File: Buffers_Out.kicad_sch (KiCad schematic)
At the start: 37 parts, among them U6 NE5532, U7 NE5532, X1 PEDAL_COMBO_TOP

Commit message: Bias voltage fix
Fixed the label for the output bias voltage.
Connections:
- net VBIAS_OUT is gone; now on net +VBIAS_OUT: C34.2, C35.2, R21.2, R23.2, R28.2, R29.2
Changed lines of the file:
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@@
 		)
 	)
-	(global_label "VBIAS_OUT"
+	(global_label "+VBIAS_OUT"
 		(shape input)
 		(at 90.17 151.13 0)
@@
 		)
 		(property "Intersheetrefs" "${INTERSHEET_REFS}"
-			(at 103.0129 151.13 0)
+			(at 104.5853 151.13 0)
 			(effects
 				(font
@@
 		)
 	)
-	(global_label "VBIAS_OUT"
+	(global_label "+VBIAS_OUT"
 		(shape input)
 		(at 90.17 81.28 0)
@@
 		)
 		(property "Intersheetrefs" "${INTERSHEET_REFS}"
-			(at 103.0129 81.28 0)
+			(at 104.5853 81.28 0)
 			(effects
 				(font

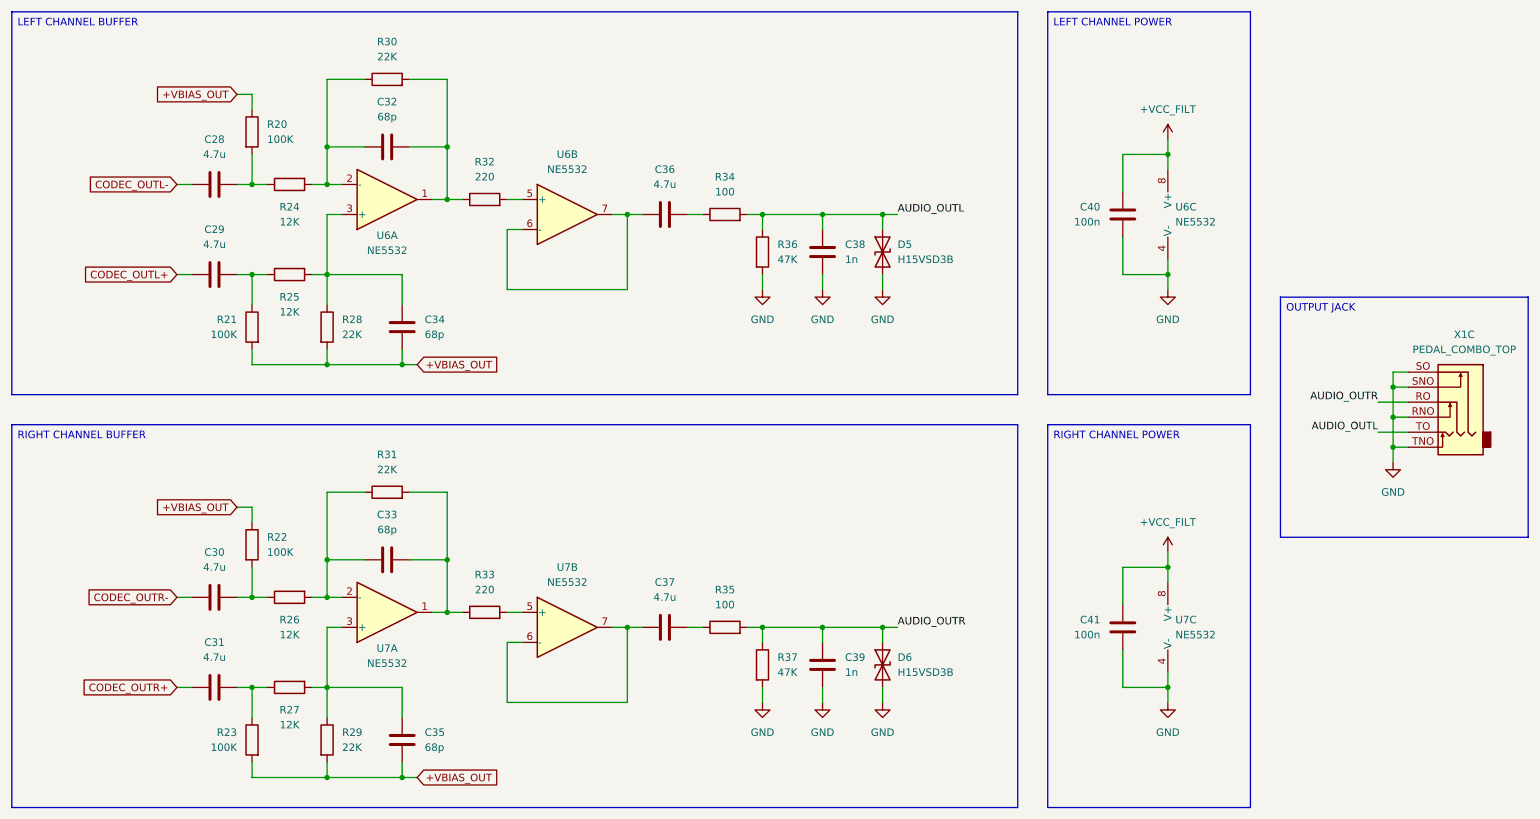
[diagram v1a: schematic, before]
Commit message: Buffer and layout
Updated the input and output buffers.
Updated the board layout.
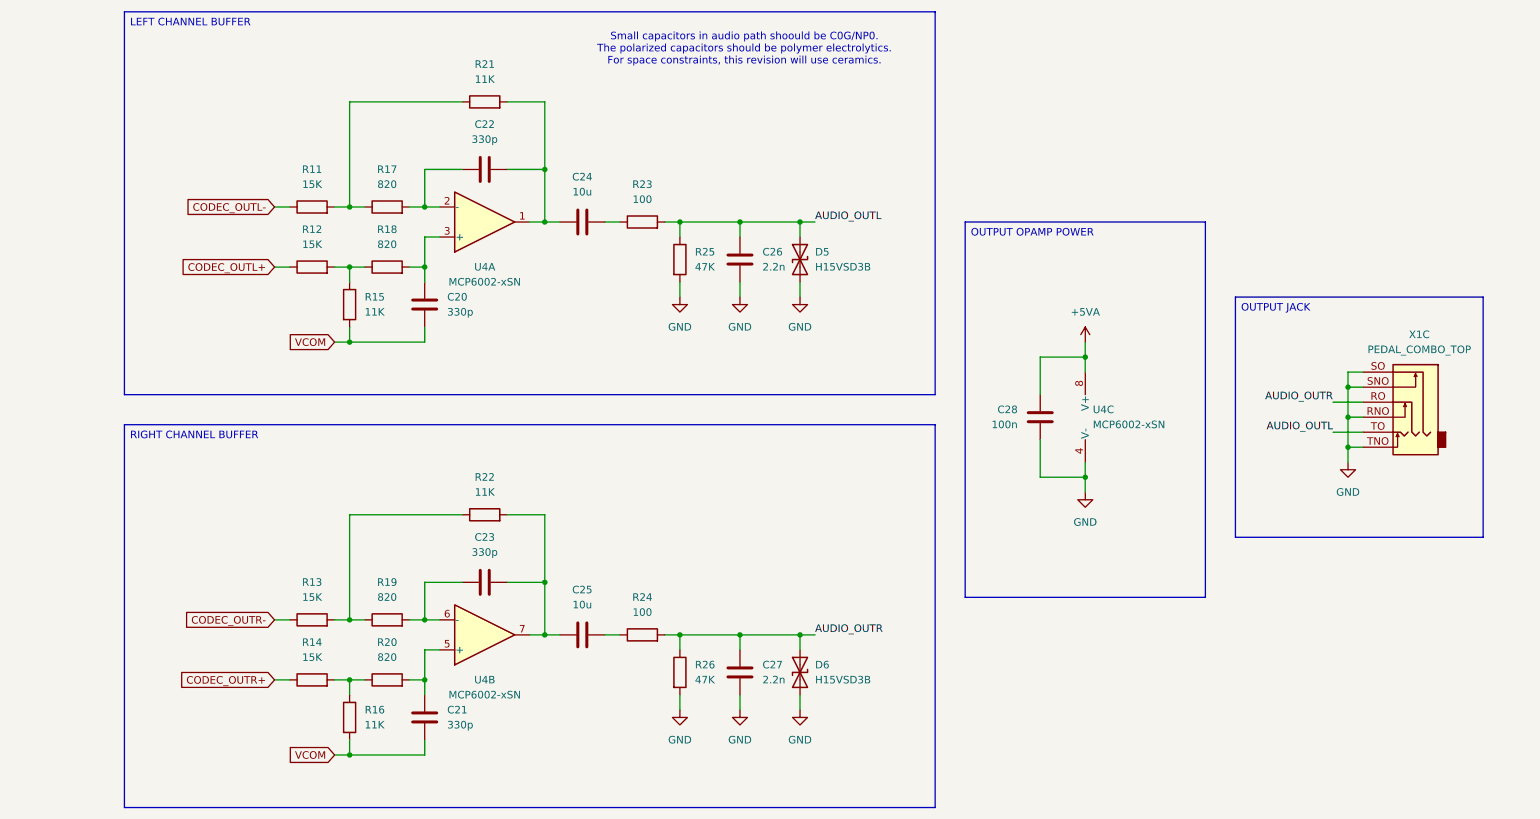
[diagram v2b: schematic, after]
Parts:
- removed C29, C30, C31, C36, C37: 4.7u, Capacitor_SMD:C_1206_3216Metric, symbol Device:C
- removed C32, C33, C34, C35: 68p, Capacitor_SMD:C_0603_1608Metric, symbol Device:C
- removed C38, C39: 1n, Capacitor_SMD:C_0603_1608Metric, symbol Device:C
- removed C40, C41: 100n, Capacitor_SMD:C_0603_1608Metric, symbol Device:C
- removed R27: 12K, Resistor_SMD:R_0603_1608Metric, symbol Device:R
- removed R28, R29, R30, R31: 22K, Resistor_SMD:R_0603_1608Metric, symbol Device:R
- removed R32, R33: 220, Resistor_SMD:R_0603_1608Metric, symbol Device:R
- removed R34, R35: 100, Resistor_SMD:R_0603_1608Metric, symbol Device:R
- removed R36, R37: 47K, Resistor_SMD:R_0603_1608Metric, symbol Device:R
- removed U6, U7: NE5532, Package_SO:SOIC-8_3.9x4.9mm_P1.27mm, symbol Amplifier_Operational:NE5532
- added C20, C21, C22, C23: 330p, Capacitor_SMD:C_0603_1608Metric, symbol Device:C
- added C24, C25: 10u, Capacitor_SMD:C_1206_3216Metric, symbol Device:C
- added C26, C27: 2.2n, Capacitor_SMD:C_0805_2012Metric, symbol Device:C
- added R11, R12, R13, R14: 15K, Resistor_SMD:R_0603_1608Metric, symbol Device:R
- added R15, R16: 11K, Resistor_SMD:R_0603_1608Metric, symbol Device:R
- added R17, R18, R19: 820, Resistor_SMD:R_0603_1608Metric, symbol Device:R
- added U4: MCP6002-xSN, Package_SO:SOIC-8_3.9x4.9mm_P1.27mm, symbol Amplifier_Operational:MCP6002-xSN
- C28: value 4.7u -> 100n; footprint Capacitor_SMD:C_1206_3216Metric -> Capacitor_SMD:C_0603_1608Metric
- R20: value 100K -> 820
- R21, R22: value 100K -> 11K
- R23: value 100K -> 100
- R24: value 12K -> 100
- R25, R26: value 12K -> 47K
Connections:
- net AUDIO_OUTL: now also R23.2, R25.1, C26.1
- net AUDIO_OUTR: now also R24.2, R26.1, C27.1
- net CODEC_OUTL+: now also R12.1
- net CODEC_OUTL-: now also R11.1; no longer C28.1
- net CODEC_OUTR+: now also R14.1
- net CODEC_OUTR-: now also R13.1
- net GND: now also C28.2, R25.2, R26.2, C26.2, C27.2, U4.4 (V-)
- net at R23.1: now also C24.2
- net at R21.1: now also R11.2, R17.1; no longer R25.1
- net at R22.2: now also C23.2, C25.1, U4.7; no longer R26.1
- removed net +VBIAS_OUT: R20.1, R21.2, R22.1, R23.2
- new net: R14.2, R16.1, R20.1
- new net: C20.1, R18.2, U4.3 (+)
- new net: C22.2, C24.1, R21.2, U4.1
- new net: C22.1, R17.2, U4.2 (-)
- new net: C21.1, R20.2, U4.5 (+)
- new net: R12.2, R15.1, R18.1
- new net: R13.2, R19.1, R22.1
- new net: C23.1, R19.2, U4.6 (-)
- new net: C25.2, R24.1
- new net +5VA: C28.1, U4.8 (V+)
- new net VCOM: C20.2, C21.2, R15.2, R16.2
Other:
- note added: "Small capacitors in audio path shoould be C0G/NP0. The polarized capacitors should be polymer electrolytics. For space constraints, this revision will use ceramics."
- moved on the sheet: X1C
